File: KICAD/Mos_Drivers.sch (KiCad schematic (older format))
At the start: 15 parts, among them U12 UCC27284-Q1

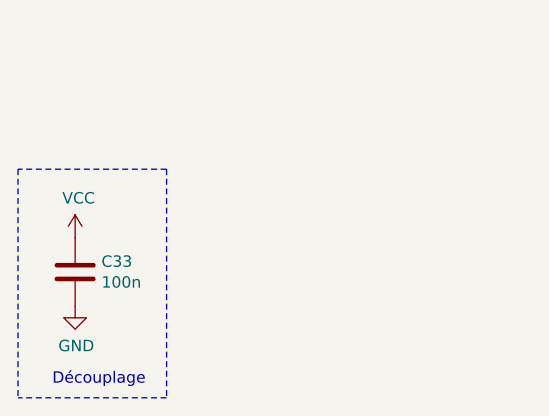
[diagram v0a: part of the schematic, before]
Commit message: end of placement 7 beginning of routing
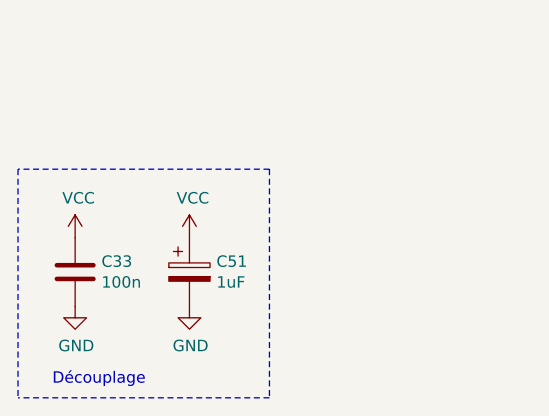
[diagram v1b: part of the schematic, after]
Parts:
- added C50: 1uF, Sesame_footprint:C_0805_2012Metric_Pad1.18x1.45mm_HandSolder, symbol Device:CP
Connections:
- net GND: now also C50.2
- net VCC: now also C50.1
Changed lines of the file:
@@
 $Descr A4 11693 8268
 encoding utf-8
-Sheet 12 17
+Sheet 15 17
 Title "SESAME"
 Date ""
@@
 L power:GND #PWR082
 U 1 1 612BD1C9
-P 850 7250
+P 1350 7250
 AR Path="/60F19D6C/612BD1C9" Ref="#PWR082"  Part="1"
 AR Path="/6187941C/612BD1C9" Ref="#PWR?"  Part="1"
 AR Path="/61996C9F/612BD1C9" Ref="#PWR?"  Part="1"
 AR Path="/619A00BB/612BD1C9" Ref="#PWR0118"  Part="1"
-F 0 "#PWR0118" H 850 7000 50  0001 C CNN
-F 1 "GND" H 855 7077 50  0000 C CNN
-F 2 "" H 850 7250 50  0001 C CNN
-F 3 "" H 850 7250 50  0001 C CNN
-	1    850  7250
+F 0 "#PWR0118" H 1350 7000 50  0001 C CNN
+F 1 "GND" H 1355 7077 50  0000 C CNN
+F 2 "" H 1350 7250 50  0001 C CNN
+F 3 "" H 1350 7250 50  0001 C CNN
+	1    1350 7250
 	1    0    0    -1
 $EndComp
@@
 	7650 3950 7650 4150
 Wire Notes Line
-	1250 6650 600  6650
+	1700 6650 600  6650
 Text Notes 750  7600 0    50   ~ 0
 Découplage
 Wire Notes Line
-	1250 7650 600  7650
+	1700 7650 600  7650
 Wire Notes Line
-	1250 6650 1250 7650
+	1700 6650 1700 7650
 Wire Notes Line
 	600  6650 600  7650
@@
 	1    0    0    -1
 $EndComp
+$Comp
+L Device:CP C50
+U 1 1 6128010B
+P 1350 7100
+AR Path="/60F19D6C/6128010B" Ref="C50"  Part="1"
+AR Path="/619A00BB/6128010B" Ref="C51"  Part="1"
+F 0 "C51" H 1468 7146 50  0000 L CNN
+F 1 "1uF" H 1468 7055 50  0000 L CNN
+F 2 "Sesame_footprint:C_0805_2012Metric_Pad1.18x1.45mm_HandSolder" H 1388 6950 50  0001 C CNN
+F 3 "~" H 1350 7100 50  0001 C CNN
+	1    1350 7100
+	1    0    0    -1
+$EndComp
+$Comp
+L power:GND #PWR030
+U 1 1 61281713
+P 850 7250
+AR Path="/60F19D6C/61281713" Ref="#PWR030"  Part="1"
+AR Path="/6187941C/61281713" Ref="#PWR?"  Part="1"
+AR Path="/61996C9F/61281713" Ref="#PWR?"  Part="1"
+AR Path="/619A00BB/61281713" Ref="#PWR0135"  Part="1"
+F 0 "#PWR0135" H 850 7000 50  0001 C CNN
+F 1 "GND" H 855 7077 50  0000 C CNN
+F 2 "" H 850 7250 50  0001 C CNN
+F 3 "" H 850 7250 50  0001 C CNN
+	1    850  7250
+	1    0    0    -1
+$EndComp
+$Comp
+L power:VCC #PWR0134
+U 1 1 61281BBD
+P 1350 6950
+AR Path="/60F19D6C/61281BBD" Ref="#PWR0134"  Part="1"
+AR Path="/6187941C/61281BBD" Ref="#PWR?"  Part="1"
+AR Path="/61996C9F/61281BBD" Ref="#PWR?"  Part="1"
+AR Path="/619A00BB/61281BBD" Ref="#PWR0136"  Part="1"
+F 0 "#PWR0136" H 1350 6800 50  0001 C CNN
+F 1 "VCC" H 1365 7123 50  0000 C CNN
+F 2 "" H 1350 6950 50  0001 C CNN
+F 3 "" H 1350 6950 50  0001 C CNN
+	1    1350 6950
+	1    0    0    -1
+$EndComp

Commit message: 200 conn. remaining
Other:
- note added: "cap 100v"
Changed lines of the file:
@@
 $Descr A4 11693 8268
 encoding utf-8
-Sheet 15 17
+Sheet 12 17
 Title "SESAME"
 Date ""
@@
 AR Path="/61996C9F/612BC387" Ref="C?"  Part="1"
 AR Path="/619A00BB/612BC387" Ref="C33"  Part="1"
-F 0 "C33" H 965 7146 50  0000 L CNN
+F 0 "C23" H 965 7146 50  0000 L CNN
 F 1 "100n" H 965 7055 50  0000 L CNN
 F 2 "Sesame_footprint:C_0805_2012Metric_Pad1.18x1.45mm_HandSolder" H 888 6950 50  0001 C CNN
@@
 AR Path="/61996C9F/612BD1C9" Ref="#PWR?"  Part="1"
 AR Path="/619A00BB/612BD1C9" Ref="#PWR0118"  Part="1"
-F 0 "#PWR0118" H 1350 7000 50  0001 C CNN
+F 0 "#PWR082" H 1350 7000 50  0001 C CNN
 F 1 "GND" H 1355 7077 50  0000 C CNN
 F 2 "" H 1350 7250 50  0001 C CNN
@@
 AR Path="/61996C9F/612BD72C" Ref="#PWR?"  Part="1"
 AR Path="/619A00BB/612BD72C" Ref="#PWR0120"  Part="1"
-F 0 "#PWR0120" H 4400 3900 50  0001 C CNN
+F 0 "#PWR084" H 4400 3900 50  0001 C CNN
 F 1 "GND" H 4405 3977 50  0000 C CNN
 F 2 "" H 4400 4150 50  0001 C CNN
@@
 AR Path="/61996C9F/612C2683" Ref="#PWR?"  Part="1"
 AR Path="/619A00BB/612C2683" Ref="#PWR0121"  Part="1"
-F 0 "#PWR0121" H 6050 4100 50  0001 C CNN
+F 0 "#PWR085" H 6050 4100 50  0001 C CNN
 F 1 "GND" H 6055 4177 50  0000 C CNN
 F 2 "" H 6050 4350 50  0001 C CNN
@@
 AR Path="/61996C9F/612C31FB" Ref="D?"  Part="1"
 AR Path="/619A00BB/612C31FB" Ref="D15"  Part="1"
-F 0 "D15" V 6004 3380 50  0000 L CNN
+F 0 "D8" V 6004 3380 50  0000 L CNN
 F 1 "SS36" V 6095 3380 50  0000 L CNN
 F 2 "Diode_SMD:D_SMA_Handsoldering" H 6050 3300 50  0001 C CNN
@@
 AR Path="/61996C9F/6157FC90" Ref="#PWR?"  Part="1"
 AR Path="/619A00BB/6157FC90" Ref="#PWR0117"  Part="1"
-F 0 "#PWR0117" H 850 6800 50  0001 C CNN
+F 0 "#PWR081" H 850 6800 50  0001 C CNN
 F 1 "VCC" H 865 7123 50  0000 C CNN
 F 2 "" H 850 6950 50  0001 C CNN
@@
 AR Path="/61996C9F/6154F3B3" Ref="TP?"  Part="1"
 AR Path="/619A00BB/6154F3B3" Ref="TP46"  Part="1"
-F 0 "TP46" H 8250 3850 50  0000 L CNN
+F 0 "TP33" H 8250 3850 50  0000 L CNN
 F 1 "TP_POP" H 8300 3750 50  0000 C CNN
 F 2 "TestPoint:TestPoint_Loop_D1.80mm_Drill1.0mm_Beaded" H 8300 3650 50  0001 C CNN
@@
 AR Path="/61996C9F/61556ADA" Ref="TP?"  Part="1"
 AR Path="/619A00BB/61556ADA" Ref="TP47"  Part="1"
-F 0 "TP47" H 8250 4150 50  0000 L CNN
+F 0 "TP34" H 8250 4150 50  0000 L CNN
 F 1 "TP_POP" H 8300 4050 50  0000 C CNN
 F 2 "TestPoint:TestPoint_Loop_D1.80mm_Drill1.0mm_Beaded" H 8300 3950 50  0001 C CNN
@@
 AR Path="/61996C9F/61556D55" Ref="TP?"  Part="1"
 AR Path="/619A00BB/61556D55" Ref="TP45"  Part="1"
-F 0 "TP45" H 8250 3150 50  0000 L CNN
+F 0 "TP32" H 8250 3150 50  0000 L CNN
 F 1 "TP_POP" H 8300 3050 50  0000 C CNN
 F 2 "TestPoint:TestPoint_Loop_D1.80mm_Drill1.0mm_Beaded" H 8300 2950 50  0001 C CNN
@@
 AR Path="/61996C9F/615F8500" Ref="U?"  Part="1"
 AR Path="/619A00BB/615F8500" Ref="U17"  Part="1"
-F 0 "U17" H 4000 4250 50  0000 C CNN
+F 0 "U12" H 4000 4250 50  0000 C CNN
 F 1 "UCC27284-Q1" H 4000 4150 50  0000 C CNN
 F 2 "Package_SO:SOIC-8_3.9x4.9mm_P1.27mm" H 4400 3450 50  0001 C CNN
@@
 AR Path="/61996C9F/615FA578" Ref="#PWR?"  Part="1"
 AR Path="/619A00BB/615FA578" Ref="#PWR0119"  Part="1"
-F 0 "#PWR0119" H 4400 2600 50  0001 C CNN
+F 0 "#PWR083" H 4400 2600 50  0001 C CNN
 F 1 "VCC" H 4415 2923 50  0000 C CNN
 F 2 "" H 4400 2750 50  0001 C CNN
@@
 AR Path="/61996C9F/617A570A" Ref="D?"  Part="1"
 AR Path="/619A00BB/617A570A" Ref="D16"  Part="1"
-F 0 "D16" V 6004 4280 50  0000 L CNN
+F 0 "D9" V 6004 4280 50  0000 L CNN
 F 1 "SS36" V 6095 4280 50  0000 L CNN
 F 2 "Diode_SMD:D_SMA_Handsoldering" H 6050 4200 50  0001 C CNN
@@
 AR Path="/61996C9F/617B4129" Ref="D?"  Part="1"
 AR Path="/619A00BB/617B4129" Ref="D17"  Part="1"
-F 0 "D17" H 7450 3167 50  0000 C CNN
+F 0 "D10" H 7450 3167 50  0000 C CNN
 F 1 "SS36" H 7450 3076 50  0000 C CNN
 F 2 "Diode_SMD:D_SMA_Handsoldering" H 7450 2950 50  0001 C CNN
@@
 AR Path="/61996C9F/617C4D4F" Ref="R?"  Part="1"
 AR Path="/619A00BB/617C4D4F" Ref="R85"  Part="1"
-F 0 "R85" V 6943 2950 50  0000 C CNN
+F 0 "R66" V 6943 2950 50  0000 C CNN
 F 1 "1" V 7034 2950 50  0000 C CNN
 F 2 "Sesame_footprint:R_0805_2012Metric_Pad1.20x1.40mm_HandSolder" V 7080 2950 50  0001 C CNN
@@
 AR Path="/61996C9F/617CA6D6" Ref="R?"  Part="1"
 AR Path="/619A00BB/617CA6D6" Ref="R87"  Part="1"
-F 0 "R87" V 7093 3150 50  0000 C CNN
+F 0 "R68" V 7093 3150 50  0000 C CNN
 F 1 "5" V 7184 3150 50  0000 C CNN
 F 2 "Sesame_footprint:R_0805_2012Metric_Pad1.20x1.40mm_HandSolder" V 7230 3150 50  0001 C CNN
@@
 AR Path="/60F19D6C/619F44C6" Ref="C25"  Part="1"
 AR Path="/619A00BB/619F44C6" Ref="C35"  Part="1"
-F 0 "C35" H 5818 3496 50  0000 L CNN
+F 0 "C25" H 5818 3496 50  0000 L CNN
 F 1 "1u" H 5818 3405 50  0000 L CNN
 F 2 "Sesame_footprint:C_0805_2012Metric_Pad1.18x1.45mm_HandSolder" H 5738 3300 50  0001 C CNN
@@
 AR Path="/61996C9F/61A058A4" Ref="D?"  Part="1"
 AR Path="/619A00BB/61A058A4" Ref="D18"  Part="1"
-F 0 "D18" H 7450 4167 50  0000 C CNN
+F 0 "D11" H 7450 4167 50  0000 C CNN
 F 1 "SS36" H 7450 4076 50  0000 C CNN
 F 2 "Diode_SMD:D_SMA_Handsoldering" H 7450 3950 50  0001 C CNN
@@
 AR Path="/61996C9F/61A058AA" Ref="R?"  Part="1"
 AR Path="/619A00BB/61A058AA" Ref="R86"  Part="1"
-F 0 "R86" V 6943 3950 50  0000 C CNN
+F 0 "R67" V 6943 3950 50  0000 C CNN
 F 1 "1" V 7034 3950 50  0000 C CNN
 F 2 "Sesame_footprint:R_0805_2012Metric_Pad1.20x1.40mm_HandSolder" V 7080 3950 50  0001 C CNN
@@
 AR Path="/61996C9F/61A058B0" Ref="R?"  Part="1"
 AR Path="/619A00BB/61A058B0" Ref="R88"  Part="1"
-F 0 "R88" V 7093 4150 50  0000 C CNN
+F 0 "R69" V 7093 4150 50  0000 C CNN
 F 1 "5" V 7184 4150 50  0000 C CNN
 F 2 "Sesame_footprint:R_0805_2012Metric_Pad1.20x1.40mm_HandSolder" V 7230 4150 50  0001 C CNN
@@
 AR Path="/61996C9F/61A06D05" Ref="C?"  Part="1"
 AR Path="/619A00BB/61A06D05" Ref="C34"  Part="1"
-F 0 "C34" H 5315 3496 50  0000 L CNN
+F 0 "C24" H 5315 3496 50  0000 L CNN
 F 1 "100n" H 5315 3405 50  0000 L CNN
 F 2 "Sesame_footprint:C_0805_2012Metric_Pad1.18x1.45mm_HandSolder" H 5238 3300 50  0001 C CNN
@@
 AR Path="/60F19D6C/6128010B" Ref="C50"  Part="1"
 AR Path="/619A00BB/6128010B" Ref="C51"  Part="1"
-F 0 "C51" H 1468 7146 50  0000 L CNN
+F 0 "C50" H 1468 7146 50  0000 L CNN
 F 1 "1uF" H 1468 7055 50  0000 L CNN
 F 2 "Sesame_footprint:C_0805_2012Metric_Pad1.18x1.45mm_HandSolder" H 1388 6950 50  0001 C CNN
@@
 AR Path="/61996C9F/61281713" Ref="#PWR?"  Part="1"
 AR Path="/619A00BB/61281713" Ref="#PWR0135"  Part="1"
-F 0 "#PWR0135" H 850 7000 50  0001 C CNN
+F 0 "#PWR030" H 850 7000 50  0001 C CNN
 F 1 "GND" H 855 7077 50  0000 C CNN
 F 2 "" H 850 7250 50  0001 C CNN
@@
 AR Path="/61996C9F/61281BBD" Ref="#PWR?"  Part="1"
 AR Path="/619A00BB/61281BBD" Ref="#PWR0136"  Part="1"
-F 0 "#PWR0136" H 1350 6800 50  0001 C CNN
+F 0 "#PWR0134" H 1350 6800 50  0001 C CNN
 F 1 "VCC" H 1365 7123 50  0000 C CNN
 F 2 "" H 1350 6950 50  0001 C CNN
@@
 	1    0    0    -1
 $EndComp
+Text Notes 5100 3200 0    100  ~ 20
+cap 100v
 $EndSCHEMATC

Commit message: cleanup silkscreen
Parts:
- added C52: 1u, Sesame_footprint:C_0805_2012Metric_Pad1.18x1.45mm_HandSolder, symbol Device:C
- added D19: MMSZ5245, Diode_SMD:D_SOD-123, symbol Device:D_Zener
- added D20, D21: SS36, Diode_SMD:D_SMA_Handsoldering, symbol Device:D_Schottky
- added R97: 10k, Sesame_footprint:R_0805_2012Metric_Pad1.20x1.40mm_HandSolder, symbol Device:R
- added TP43, TP48: TP_POP, TestPoint:TestPoint_Loop_D1.80mm_Drill1.0mm_Beaded, symbol Connector:TestPoint
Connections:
- net VCC: now also D21.2 (A)
- net VS: now also D19.2 (A)
- net at C24.1, C25.1, U12.2 (HB): now also D19.1 (K), R97.2, TP48.1
- new net: C52.2, D20.2 (A), D21.1 (K), TP43.1
- new net: D20.1 (K), R97.1
- new net VS_Opposite: C52.1
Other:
- note added: "Charge and discharge\nresistors"
- note added: "Charge pump circuit"
- note added: "ajouter power pad"
- note removed: "ajouter power pad\nVerifier que le driver peut tenir l’etat DC"
- note removed: "cap 100v"
- moved on the sheet: C24, C25, TP32, U12

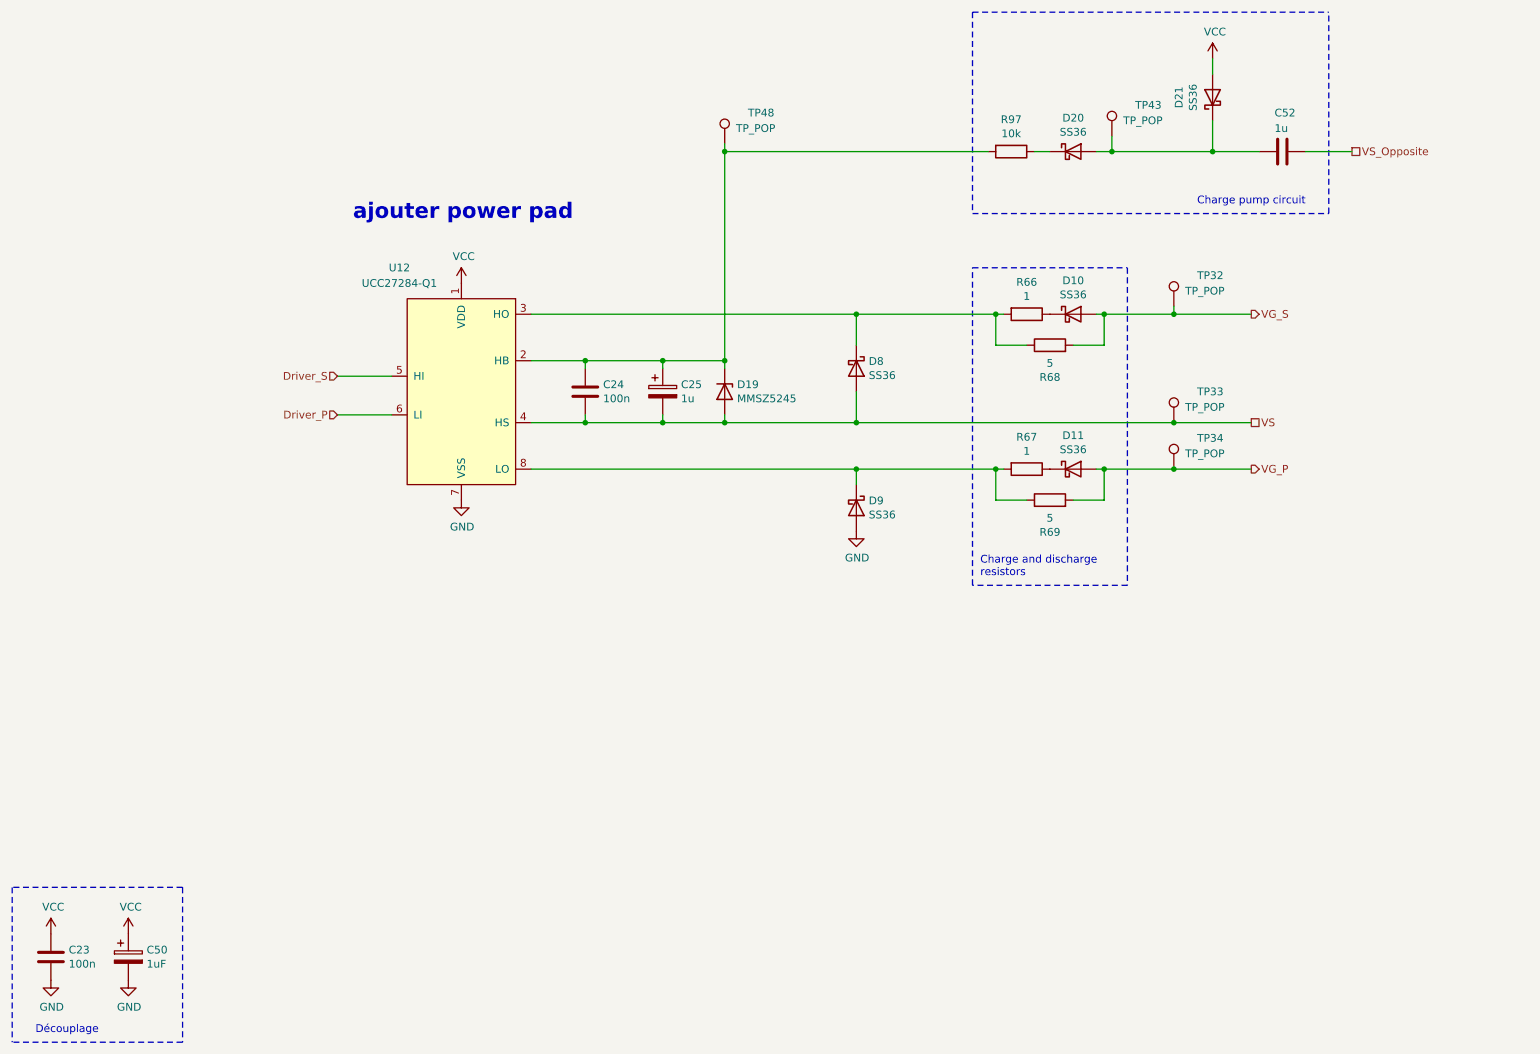
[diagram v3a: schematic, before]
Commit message: modified deadtime + added config pads on the bottom for charge pump config
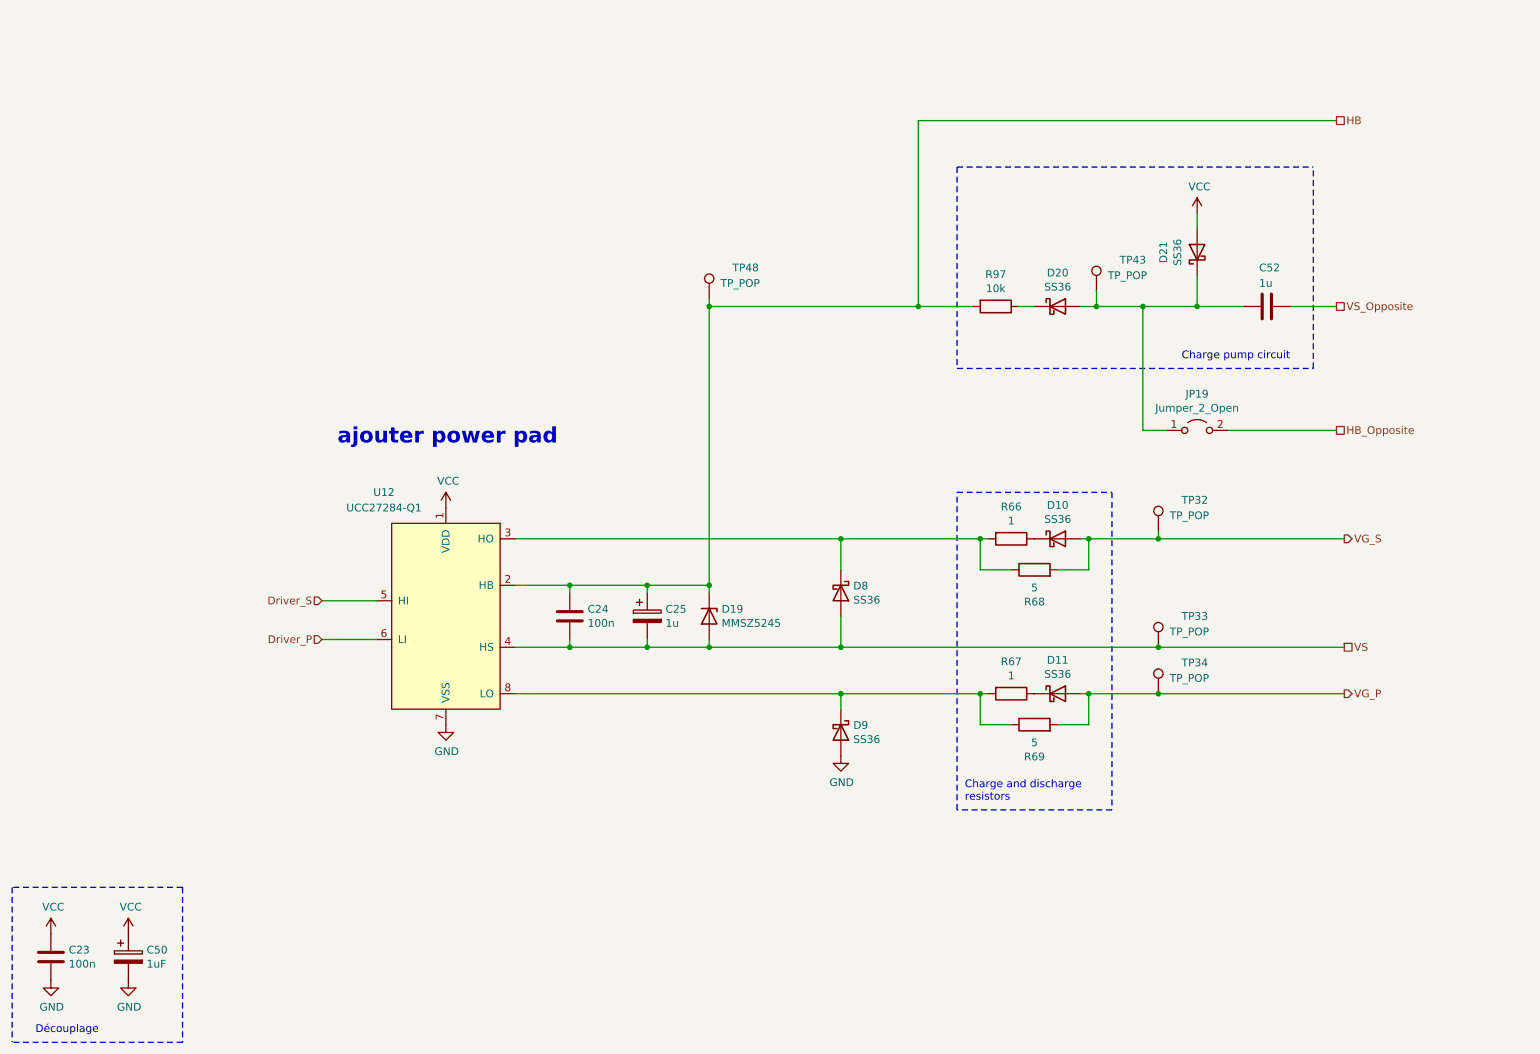
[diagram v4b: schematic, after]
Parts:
- added JP19: Jumper_2_Open, Jumper:SolderJumper-2_P1.3mm_Open_TrianglePad1.0x1.5mm, symbol Jumper:Jumper_2_Open
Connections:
- net at C52.2, D20.2 (A), D21.1 (K)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: now also JP19.1 (A)
- net HB: now reaches C24.1, C25.1, D19.1 (K), R97.2, TP48.1, U12.2 (HB)
- new net HB_Opposite: JP19.2 (B)
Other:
- moved on the sheet: C24, C25, C52, D10, D11, D19, D20, D21, D8, D9, R66, R67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
